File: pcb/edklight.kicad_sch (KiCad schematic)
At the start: 38 parts, among them J1 MotorIn, J2 ToLcd, J3 RearLight, J4 Fr Light, J5 2 But Ctrl, J6 Conn_01x01_Pin, J7 Conn_01x01_Pin, J8 Conn_01x01_Pin, J9 Conn_01x01_Pin, Q1 ZXMP4A16G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

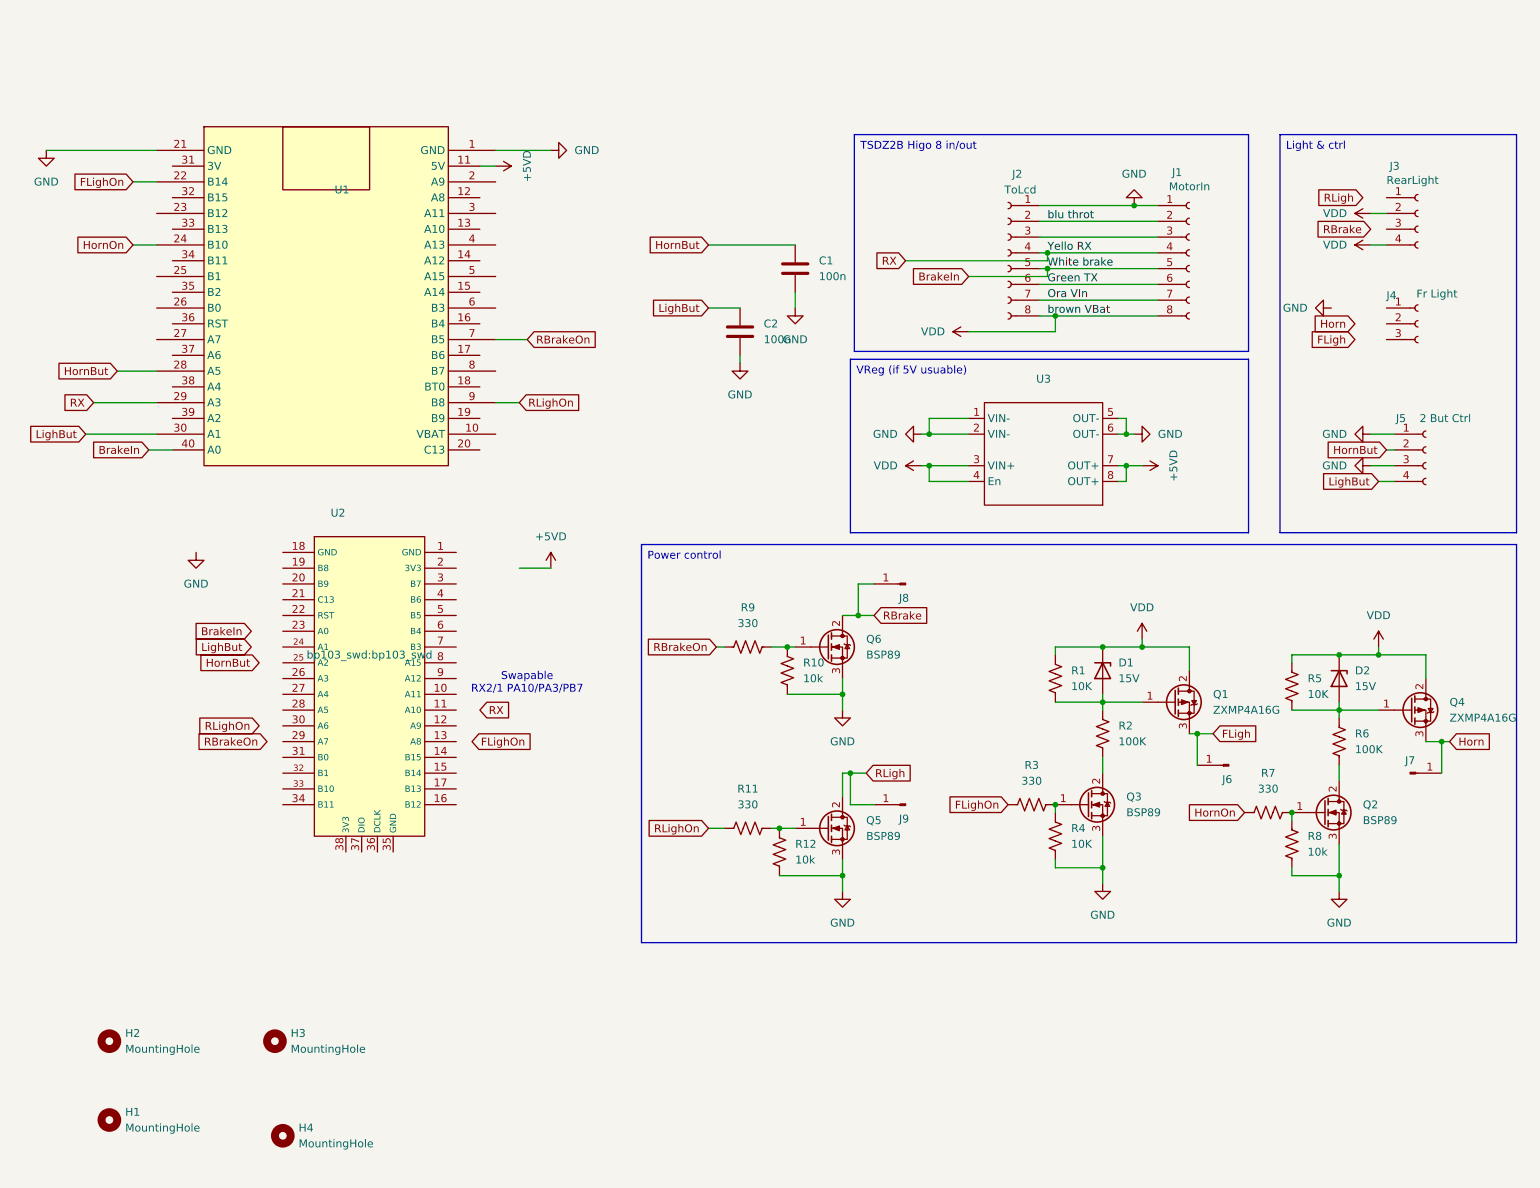
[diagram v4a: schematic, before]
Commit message: pcb : hi side mos wrong siden , chg few R+D footprint
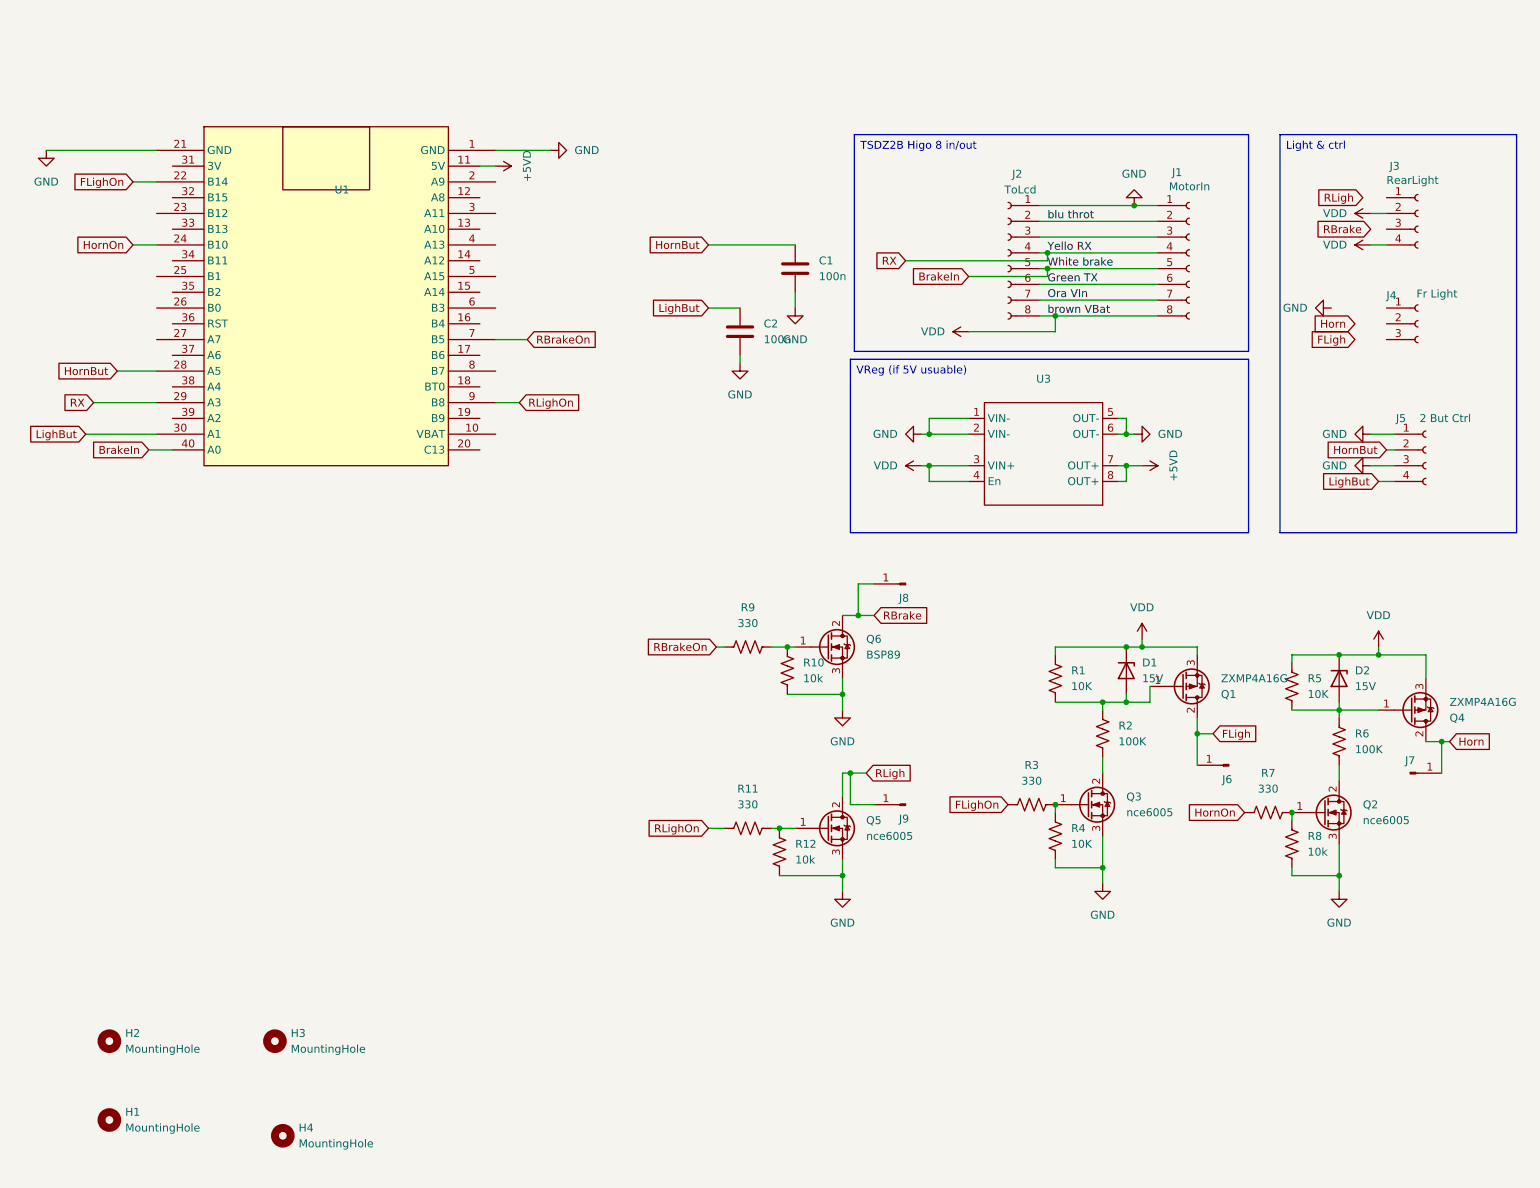
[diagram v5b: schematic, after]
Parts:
- removed U2: ~, bp103_swd:bp103_swd, symbol bp103:bp103_swd
- D1: footprint Diode_THT:D_A-405_P2.54mm_Vertical_KathodeUp -> Diode_THT:D_A-405_P5.08mm_Vertical_AnodeUp
- D2: footprint Diode_THT:D_A-405_P2.54mm_Vertical_AnodeUp -> Diode_THT:D_A-405_P5.08mm_Vertical_AnodeUp
- Q2, Q3, Q5: value BSP89 -> nce6005
- R2: footprint Resistor_THT:R_Axial_DIN0204_L3.6mm_D1.6mm_P7.62mm_Horizontal -> Resistor_THT:R_Axial_DIN0207_L6.3mm_D2.5mm_P5.08mm_Vertical
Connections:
- net FLigh: now also Q1.2 (D); no longer Q1.3 (S)
- net Horn: now also Q4.2 (D); no longer Q4.3 (S)
- net VDD: now also Q1.3 (S), Q4.3 (S); no longer Q1.2 (D), Q4.2 (D)
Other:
- note removed: "Swapable RX2/1 PA10/PA3/PB7"
- moved on the sheet: D1, Q1

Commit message: pcb change some placement inline with proto + wire con
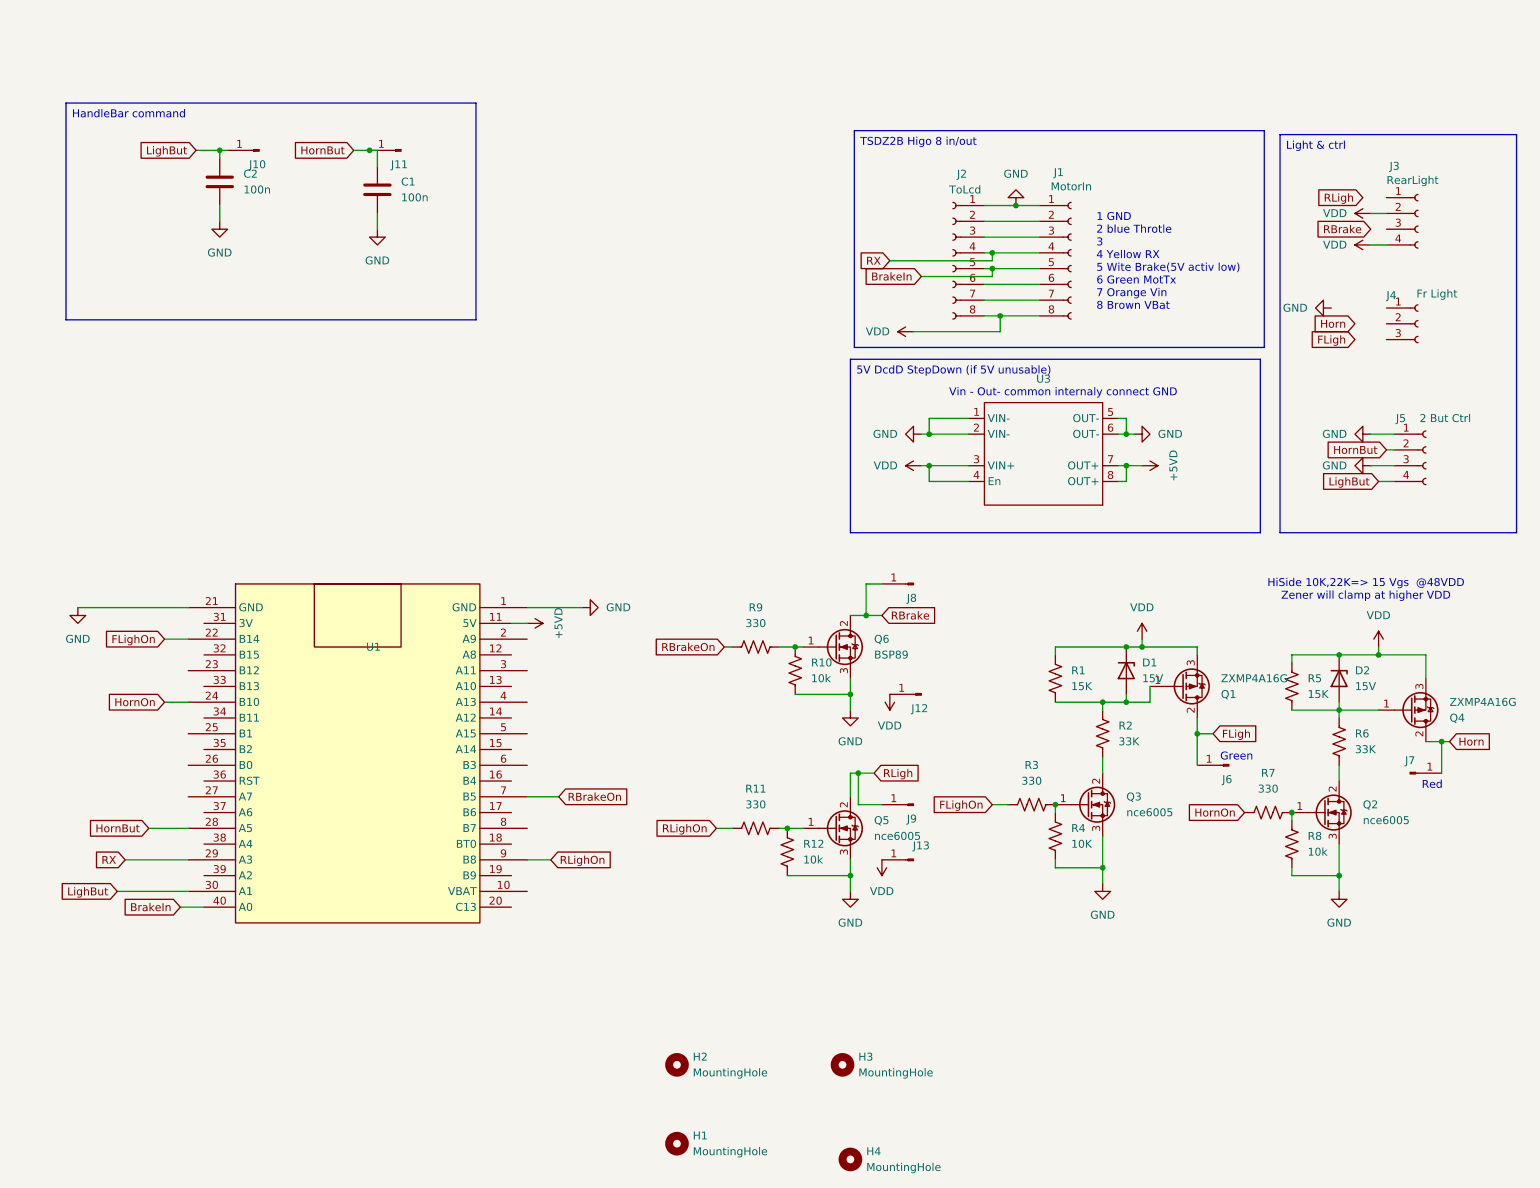
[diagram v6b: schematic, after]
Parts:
- added J10, J11, J12, J13: Conn_01x01_Pin, Connector_PinHeader_2.54mm:PinHeader_1x01_P2.54mm_Vertical, symbol Connector:Conn_01x01_Pin
- R1, R5: value 10K -> 15K
- R2, R6: value 100K -> 33K
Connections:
- net HornBut: now also J11.1 (Pin_1)
- net LighBut: now also J10.1 (Pin_1)
- net VDD: now also J12.1 (Pin_1), J13.1 (Pin_1)
- net Green TX: no longer names the net of J1.6 (Pin_6), J2.6 (Pin_6)
- net Ora VIn: no longer names the net of J1.7 (Pin_7), J2.7 (Pin_7)
- net blu throt: no longer names the net of J1.2 (Pin_2), J2.2 (Pin_2)
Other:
- note added: "1 GND 2 blue Throtle 3 4 Yellow RX 5 Wite Brake(5V activ low) 6 Green MotTx 7 Orange Vin 8 Brown VBat"
- note added: "Green"
- note added: "HiSide 10K,22K=> 15 Vgs @48VDD Zener will clamp at higher VDD"
- note added: "Red"
- note added: "Vin - Out- common internaly connect GND"
- moved on the sheet: C1, C2, H1, H2, H3, H4, J1, J2, J8, J9, Q5, Q6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

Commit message: regen new  i/o pin , brake a0 swap not 5V , new usb uart and usart swap
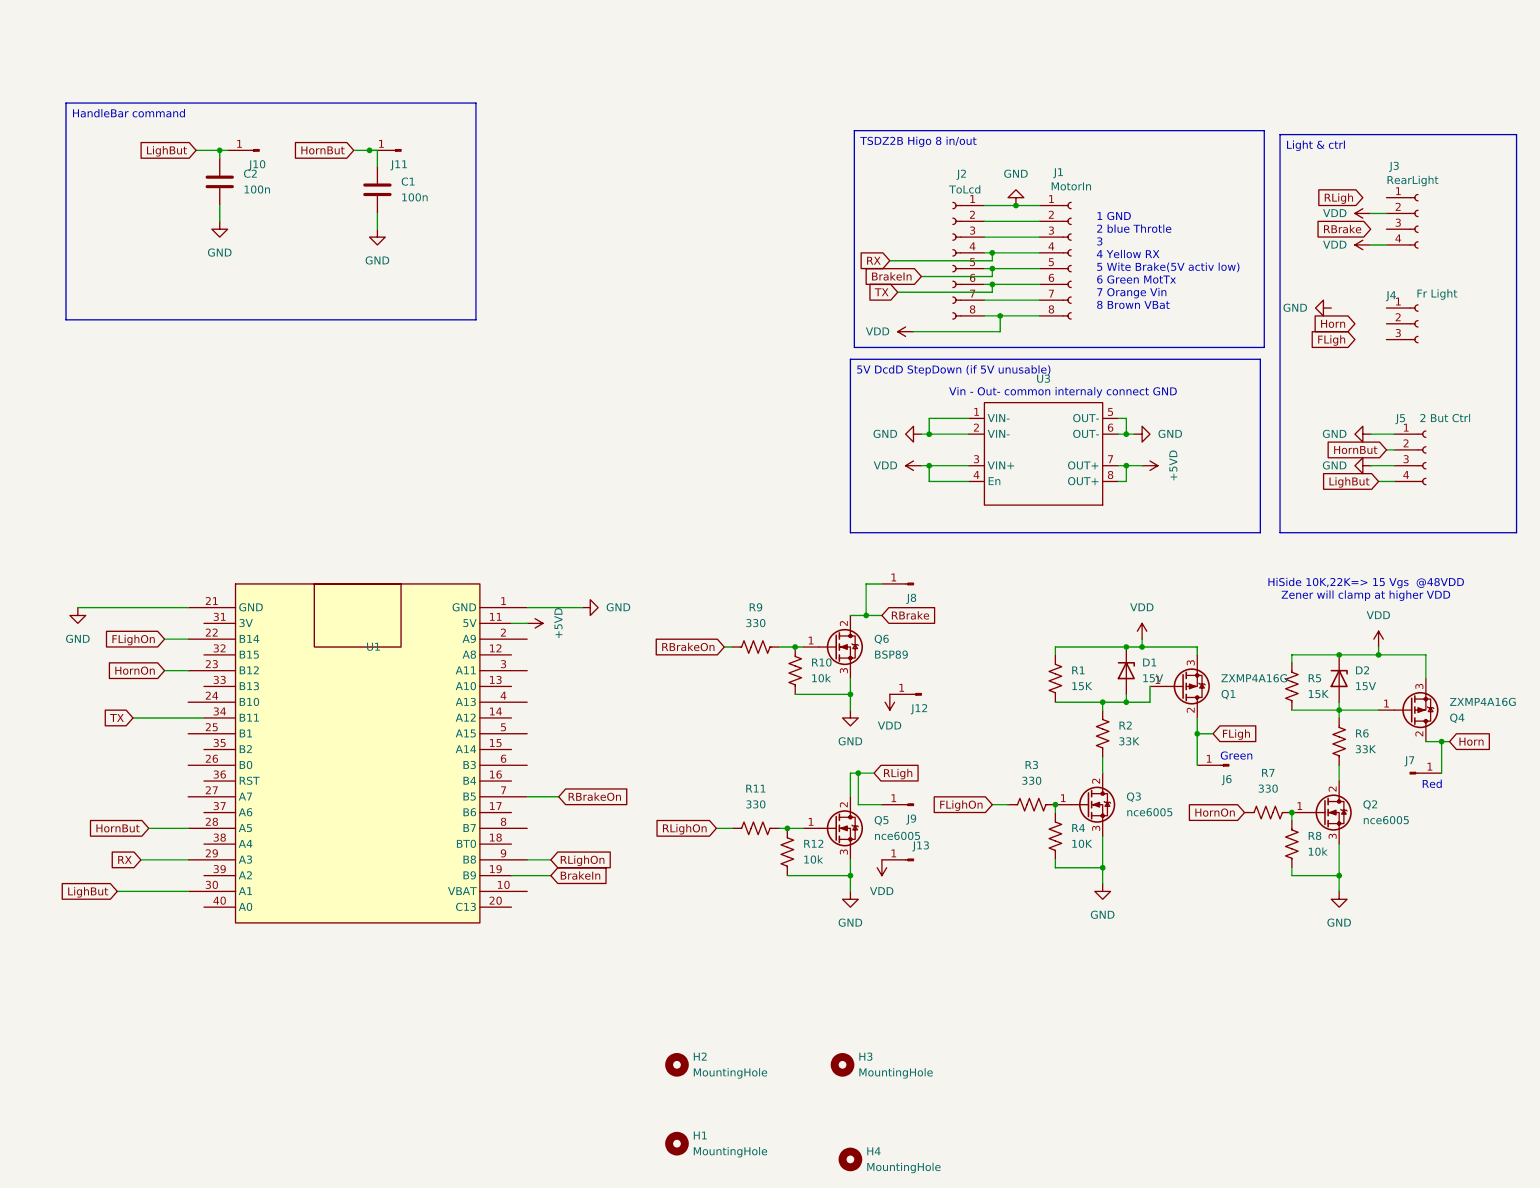
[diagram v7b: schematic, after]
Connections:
- net BrakeIn: now also U1.19 (B9); no longer U1.40 (A0)
- net HornOn: now also U1.23 (B12); no longer U1.24 (B10)
- net TX: now reaches J1.6 (Pin_6), J2.6 (Pin_6)
- net TX: now also U1.34 (B11)

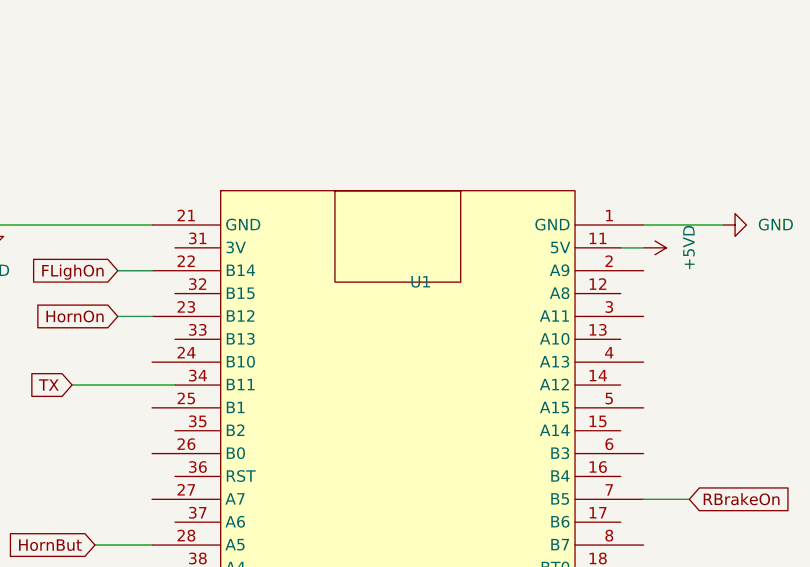
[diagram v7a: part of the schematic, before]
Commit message: regen  uart irq enable missing, switch ld to c8 , usb uart cmd wip
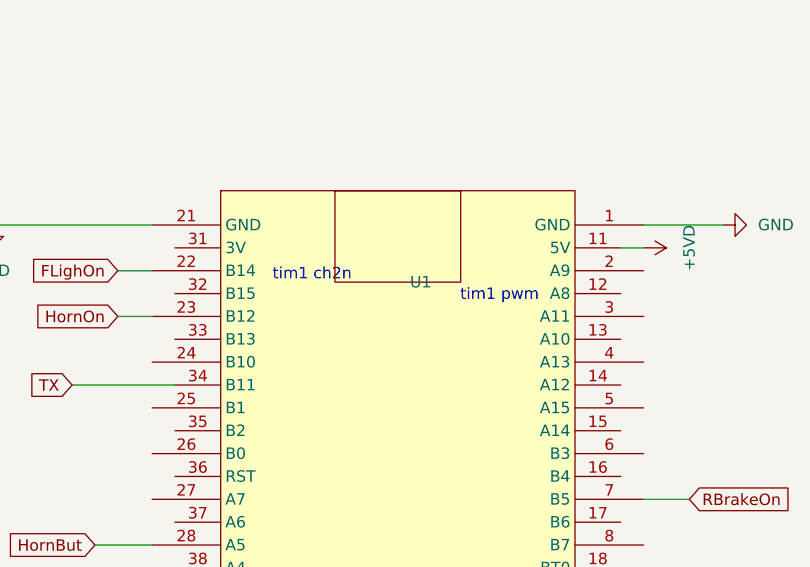
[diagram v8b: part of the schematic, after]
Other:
- note added: "tim1 ch2n"
- note added: "tim1 pwm"
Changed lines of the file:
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@@
+		)
+	)
+	(text "tim1 pwm"
+		(exclude_from_sim no)
+		(at 79.248 109.474 0)
+		(effects
+			(font
+				(size 1.27 1.27)
+			)
 		)
 	)
@@
 		(effects
 			(font
+				(size 1.27 1.27)
+			)
+		)
+	)
+	(text "tim1 ch2n"
+		(exclude_from_sim no)
+		(at 58.42 107.188 0)
+		(effects
+			(font
